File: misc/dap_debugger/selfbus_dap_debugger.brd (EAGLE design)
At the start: 35.1 x 85.1 mm, 60 parts, among them CON1 MICRO-B_U254-051N-4BH806, CON2 SHF-105-01-X-D-TH, CON3 SHF-105-01-X-D-TH, CON4 SAMTEC-LTMM-105-02-T-D, IC1 74LVC1T45GW, IC2 74LVC2G07GV, IC3 74LVC2T45DC, IC4 74LVC2T45DC, SW1 BOOT, SW2 RESET, SW3 XKB7070-Z, U1 STM32F042FX, U2 AP2112K-3.3TRG1, U3 AP2331TDW

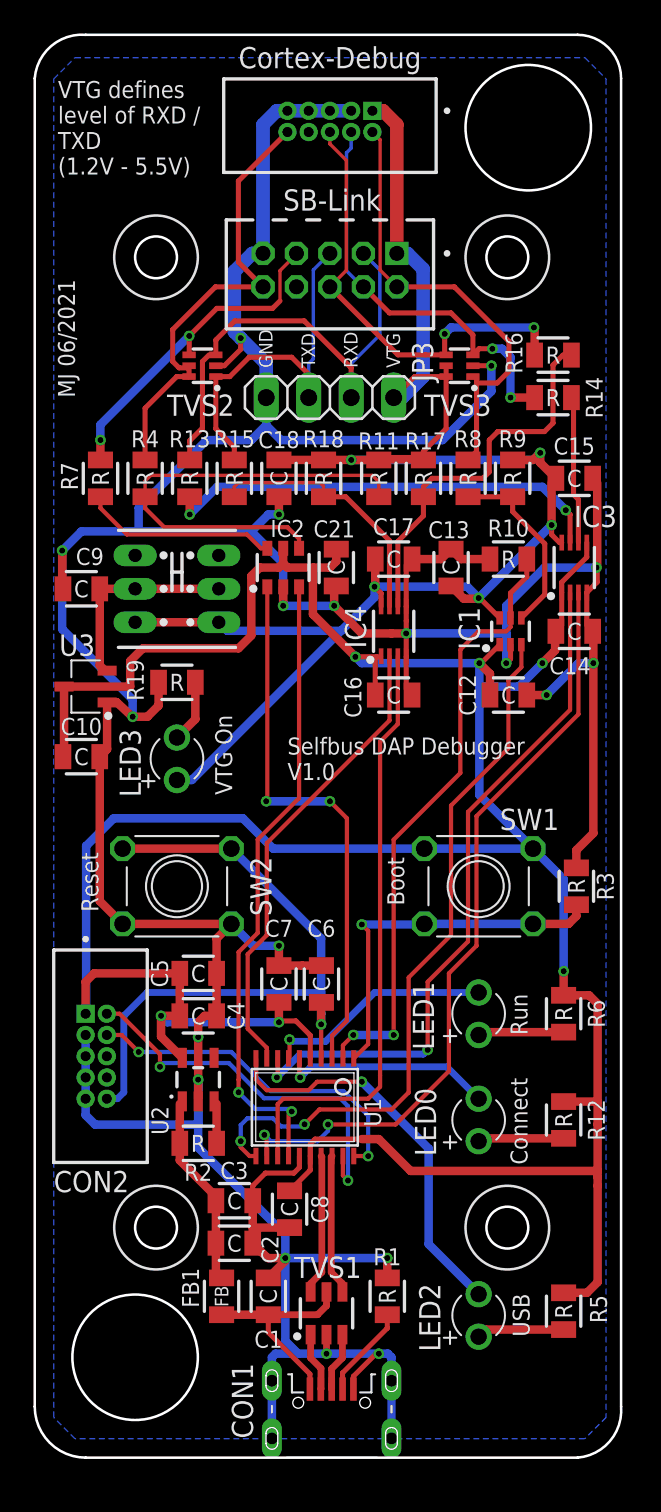
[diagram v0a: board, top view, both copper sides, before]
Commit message: Switched from Micro-USB to USB-C
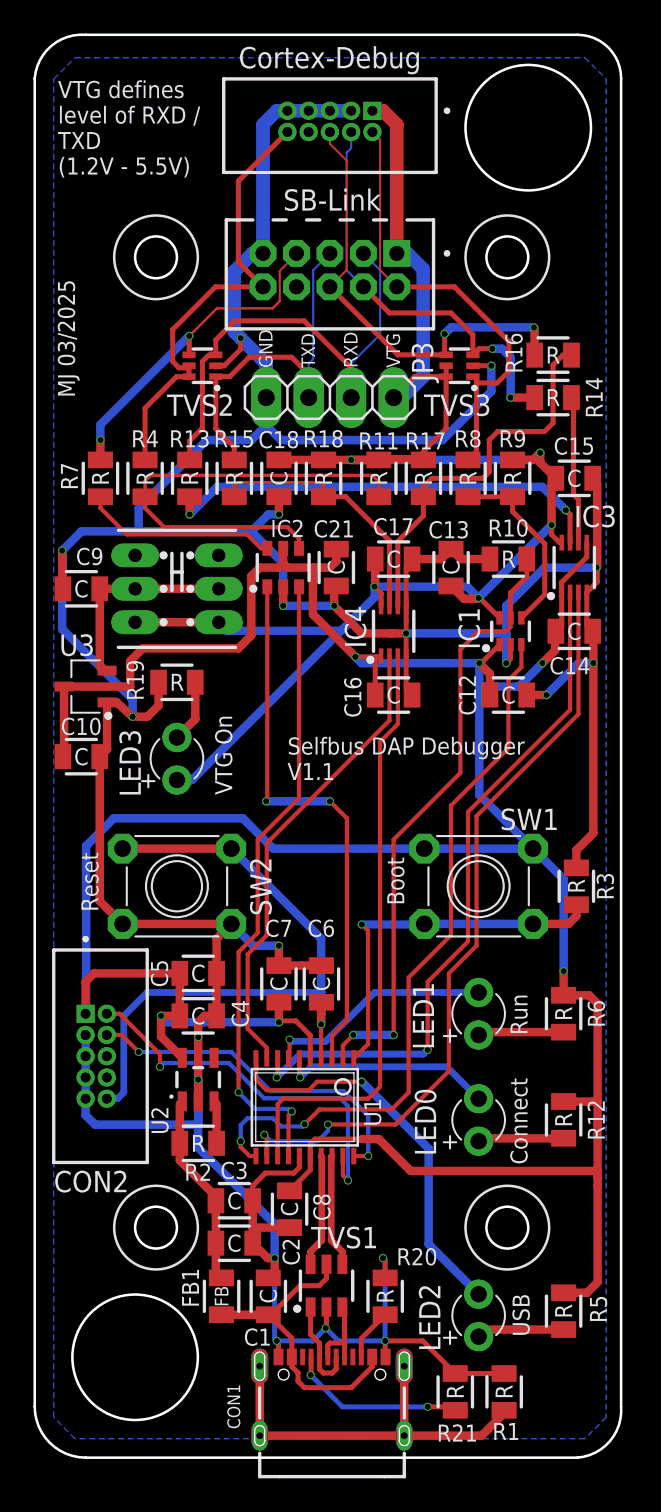
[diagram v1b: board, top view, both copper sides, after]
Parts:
- added R20, R21: 5,1k, MyRCL:R0805
- C18: value 10uF -> 10µF
- C3, C4, C5: value 4.7uF -> 4,7µF
- CON1: value MICRO-B_U254-051N-4BH806 -> XKB U262-161N-4BVC11; device MyCon-USB:U254-051N-4BH806 -> MyCon-USB:USB-C-16P-2LAYER-PADS
- R1: value 100k -> 1M
- moved R1 9.03 mm to (28.2, 4.06)
- moved CON1 6.95 mm to (13.6, 5.60)
- moved TVS1 1.65 mm to (17.6, 10.4)
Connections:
- removed net N$4: C1.1, CON1.VBUS, FB1.1, TVS1.5
- new net N$2: CON1.SHLD1, CON1.SHLD2, CON1.SHLD3, CON1.SHLD4, R1.2
- new net N$5: CON1.A5, R21.2
- new net VBUS: C1.1, CON1.VBUS1, CON1.VBUS2, FB1.1, TVS1.5
- net D_N: now also CON1.A7, CON1.B7; no longer CON1.D-
- net D_P: now also CON1.A6, CON1.B6; no longer CON1.D+
- net GND: now also CON1.GND2, R20.1, R21.1; no longer CON1.SCR@1, CON1.SCR@2, CON1.SCR@3, CON1.SCR@4
- net N$3: now also CON1.B5, R20.2; no longer CON1.ID, R1.2
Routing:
- net N$2: track 0.00 -> 23.6 mm
- net VBUS: track 0.00 -> 18.4 mm
- net N$4: track 12.8 -> 0.00 mm
- net N$5: track 0.00 -> 10.6 mm, vias 0 -> 2
- net GND: track 285.1 -> 278.3 mm, vias 19 -> 20
- net N$3: track 5.55 -> 3.12 mm
- net D_N: track 3.51 -> 5.85 mm
- net USB_N: track 8.42 -> 6.77 mm
- net USB_P: track 8.42 -> 6.77 mm
- net D_P: track 3.52 -> 4.89 mm
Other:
- board text added: "MJ 03/2025"
- board text added: "Selfbus DAP Debugger V1.1"
- board text removed: "MJ 06/2021"
- board text removed: "Selfbus DAP Debugger V1.0"

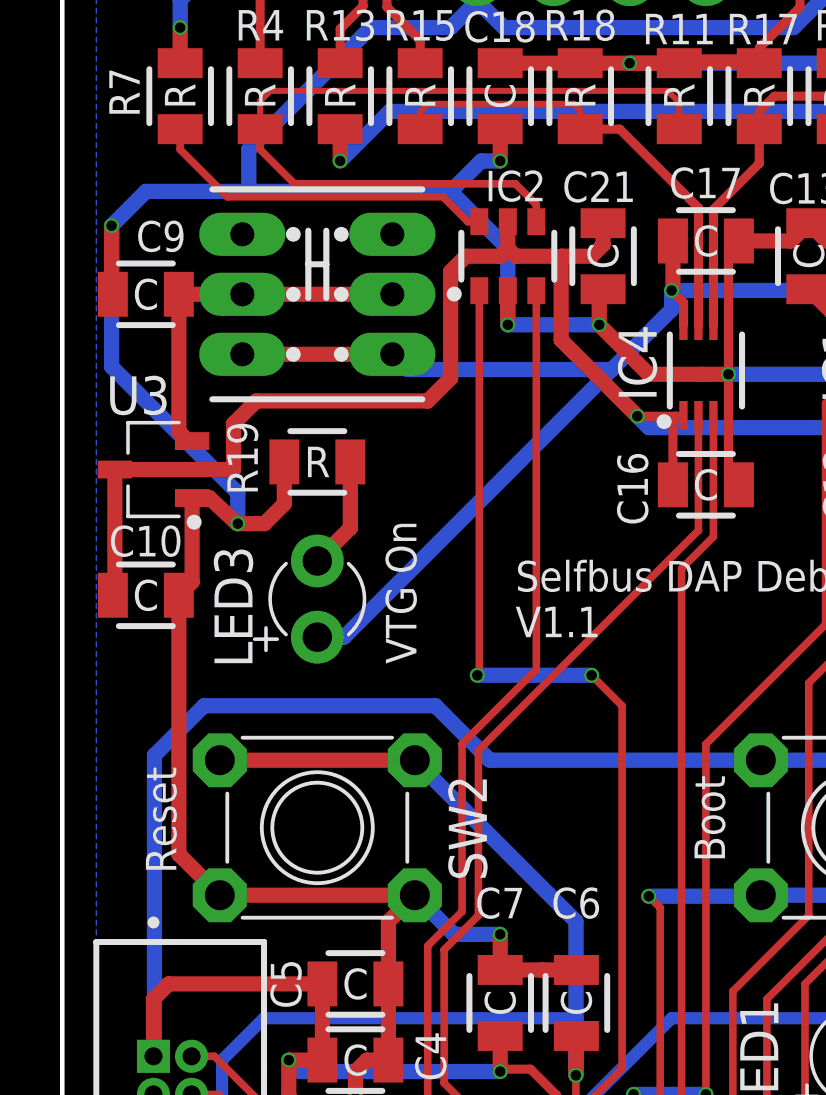
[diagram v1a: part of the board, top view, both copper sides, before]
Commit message: IC2 package switched to SOT363/SC70
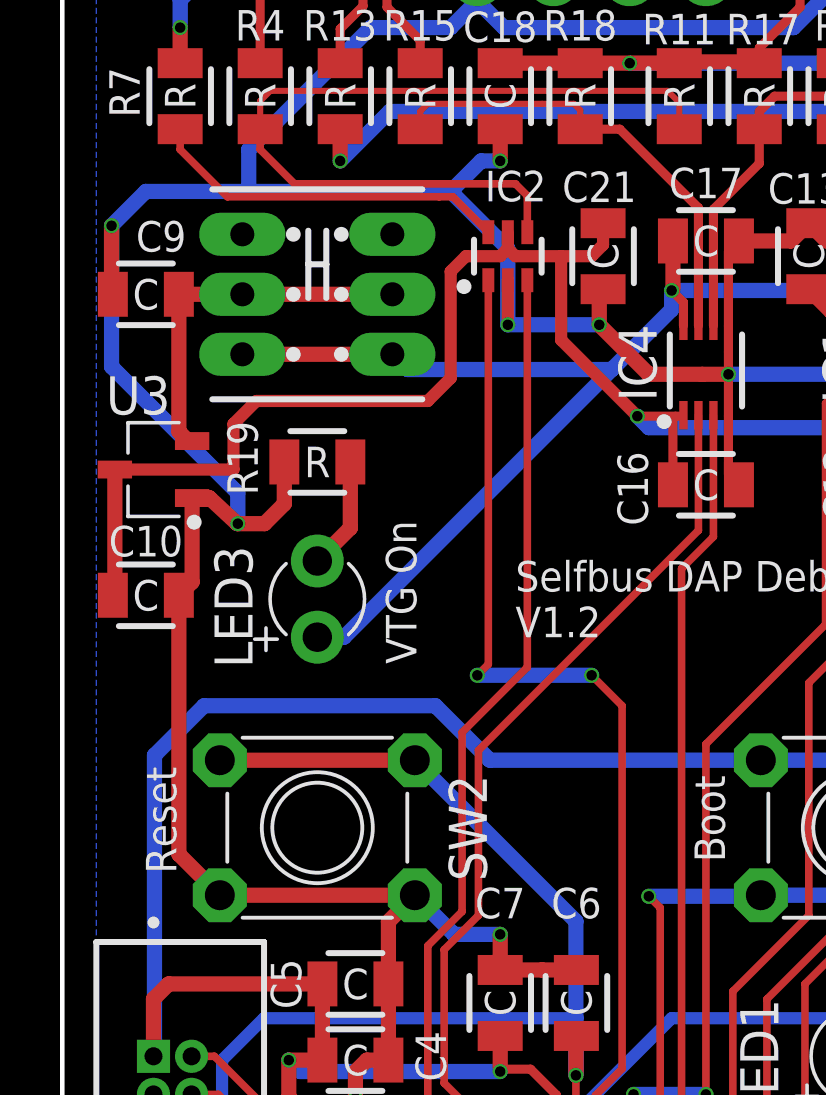
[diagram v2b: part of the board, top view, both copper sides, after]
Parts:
- IC2: value 74LVC2G07GV -> 742G07GW; device MyIC-Logic:SOT23-6 -> MyIC-Logic:SOT363
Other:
- board text added: "Selfbus DAP Debugger V1.2"
- board text removed: "Selfbus DAP Debugger V1.1"
